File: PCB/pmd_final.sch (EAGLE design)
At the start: 28 parts, among them IC1 MEGA128-A, IC4 REG1117, J1 DCJ0202, J2 RCA-LOCK, J3 RCA-LOCK, Q1 16 MHz

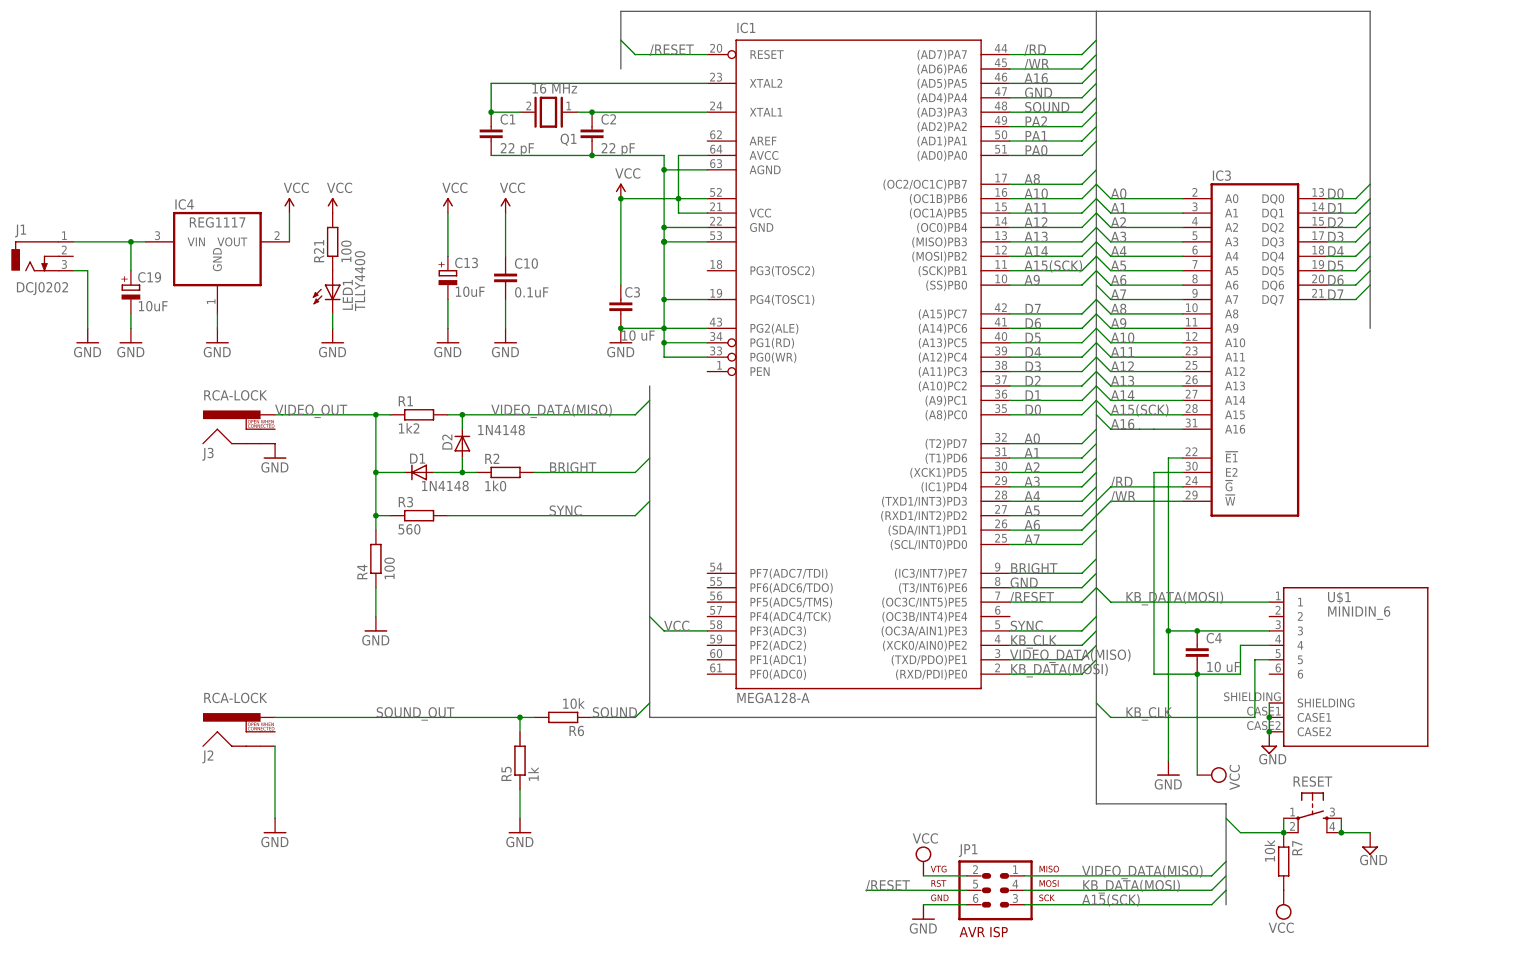
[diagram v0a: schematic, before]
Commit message: fixed 2021 version
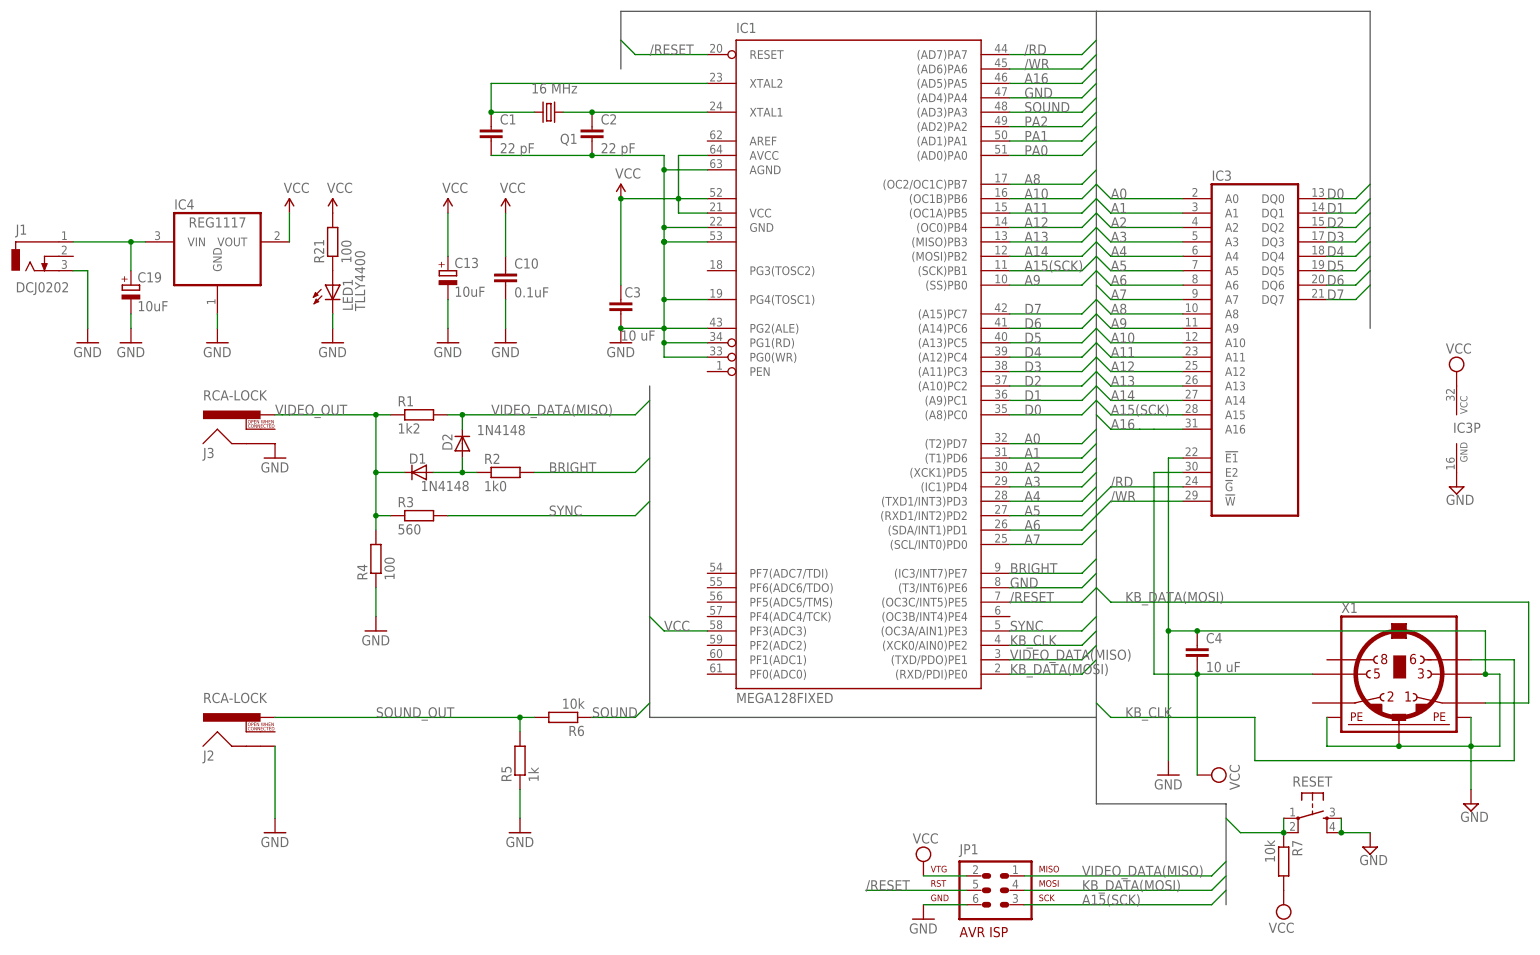
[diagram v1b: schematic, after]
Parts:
- removed U$1: MINIDIN_6, connectors-digital:MINIDIN_6
- added X1: (no value), mini_din:MINI_DIN_6
- IC1: value MEGA128-A -> MEGA128FIXED; device avr:MEGA128-A -> avr:MEGA128FIXED
- IC3: device memory-sram:MCM6226ANORMAL -> my_memory:MCM6226AULTRAWIDE
- Q1: device special:XTAL/S -> crystal:CRYSTALHC49UP
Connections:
- net GND: now also IC3P.GND, X1.3, X1.PE1, X1.PE2, X1.PE3; no longer U$1.3, U$1.CASE1, U$1.CASE2, U$1.SHIELDING
- net KB_CLK: now also X1.6; no longer U$1.5
- net KB_DATA(MOSI): now also X1.1; no longer U$1.1
- net VCC: now also IC3P.VCC, X1.5; no longer U$1.4
